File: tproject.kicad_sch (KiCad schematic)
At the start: 0 parts

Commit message: Restore original schematic and project files
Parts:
- added C1, C2, C3, C4: 100n, symbol Device:C
- added C5: 10u, symbol Device:C
- added C6: 10n, symbol Device:C
- added C7, C8: 1u, symbol Device:C
- added FB1: 120R, symbol Device:FerriteBead
- added U1: STM32F103C8T6, Package_QFP:LQFP-48_7x7mm_P0.5mm, symbol MCU_ST_STM32F1:STM32F103C8Tx
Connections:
- new net +3.3V: C1.1, C2.1, C3.1, C4.1, C5.1, C8.1, FB1.2, U1.1 (VBAT), U1.24 (VDD), U1.36 (VDD), U1.48 (VDD)
- new net +3.3VA: C6.1, C7.1, FB1.1, U1.9 (VDDA)
- new net GND: C1.2, C2.2, C3.2, C4.2, C5.2, C6.2, C7.2, C8.2, U1.23 (VSS), U1.35 (VSS), U1.47 (VSS), U1.8 (VSSA)

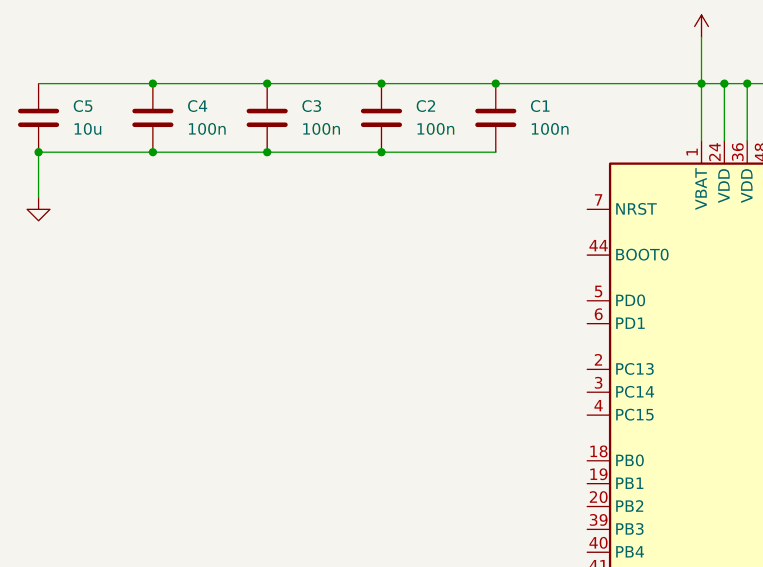
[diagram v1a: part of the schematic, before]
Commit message: Add NRST filter and BOOT0 switch circuit (C9, R1, SW1)
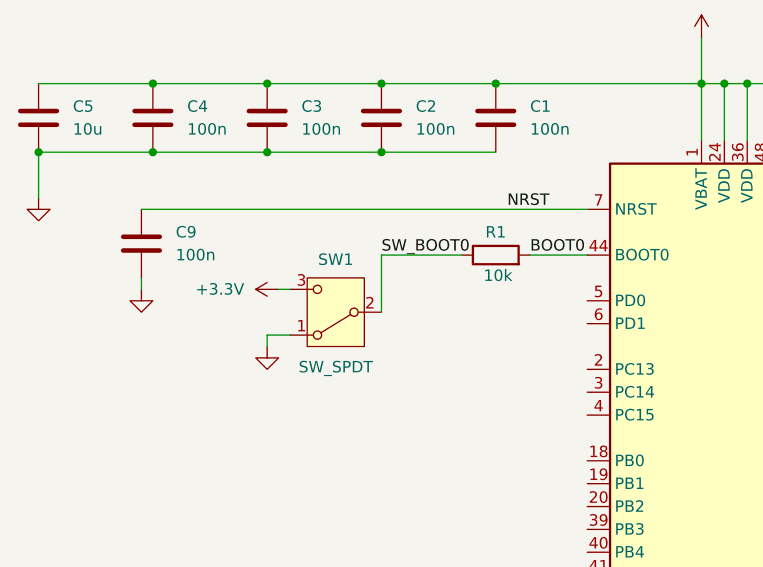
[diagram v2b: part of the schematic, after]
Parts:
- added C9: 100n, symbol Device:C
- added R1: 10k, symbol Device:R
- added SW1: SW_SPDT, symbol Switch:SW_SPDT
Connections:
- net +3.3V: now also SW1.3 (C)
- net GND: now also C9.2, SW1.1 (A)
- net BOOT0: now reaches U1.44 (BOOT0)
- net BOOT0: now also R1.2
- net NRST: now reaches U1.7 (NRST)
- net NRST: now also C9.1
- new net SW_BOOT0: R1.1, SW1.2 (B)

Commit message: Add HSE crystal oscillator circuit (Y1 16MHz, C10/C11 10p) and design note 0003
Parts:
- added C10, C11: 10p, symbol Device:C
- added Y1: 16MHz, symbol Device:Crystal_GND24
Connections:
- net GND: now also C10.2, C11.2, Y1.2 (G), Y1.4 (G)
- net USB_D-: now reaches U1.32 (PA11)
- net USB_D+: now reaches U1.33 (PA12)
- net SDIO: now reaches U1.34 (PA13)
- net SWCLK: now reaches U1.37 (PA14)
- net HSE_IN: now reaches U1.5 (PD0)
- net HSE_IN: now also C11.1, Y1.1
- net HSE_OUT: now reaches U1.6 (PD1)
- net HSE_OUT: now also C10.1, Y1.3

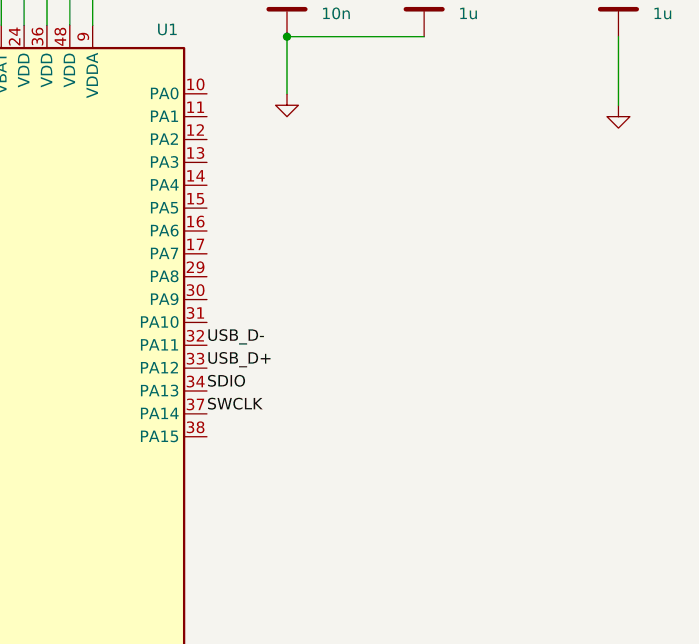
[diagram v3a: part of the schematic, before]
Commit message: Add USB Micro-B interface circuit (J1, R2 1k5 D+ pull-up) and design note 0004
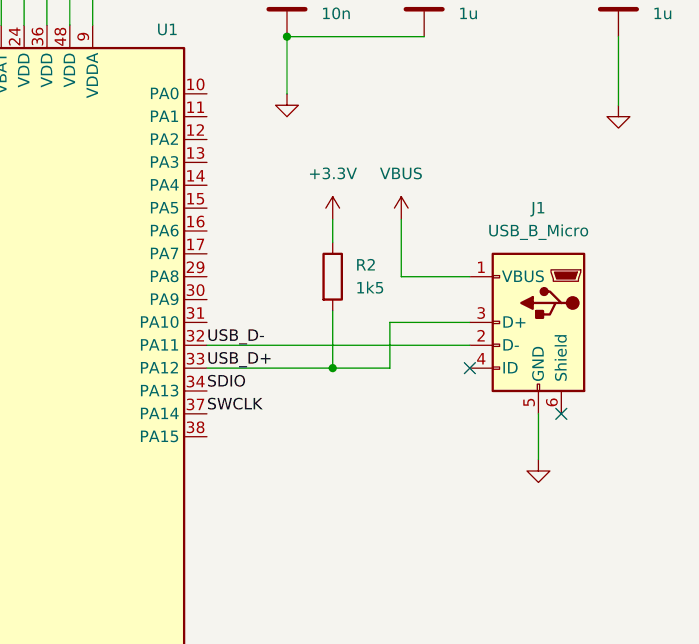
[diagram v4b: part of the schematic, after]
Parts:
- added J1: USB_B_Micro, symbol Connector:USB_B_Micro
- added R2: 1k5, symbol Device:R
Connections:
- net +3.3V: now also R2.1
- net GND: now also J1.5 (GND)
- net USB_D+: now also J1.3 (D+), R2.2
- net USB_D-: now also J1.2 (D-)
- new net VBUS: J1.1 (VBUS)
- no-connect marks 0 -> 2

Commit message: Add 3.3V LDO regulator, power LED, I2C pull-ups, and breakout connectors (U2, C12/C13, D1, R3-R5, J2-J4) and design note 0005
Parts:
- added C12, C13: 22u, symbol Device:C
- added D1: RED, symbol Device:LED
- added J2, J3, J4: Conn_01x04_Pin, symbol Connector:Conn_01x04_Pin
- added R3, R4, R5: 1k5, symbol Device:R
- added U2: AMS1117-3.3, Package_TO_SOT_SMD:SOT-223-3_TabPin2, symbol Regulator_Linear:AMS1117-3.3
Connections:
- net +3.3V: now also C12.1, D1.2 (A), J2.1 (Pin_1), J3.1 (Pin_1), J4.1 (Pin_1), R4.1, R5.1, U2.2 (VO)
- net GND: now also C12.2, C13.2, J2.4 (Pin_4), J3.4 (Pin_4), J4.4 (Pin_4), R3.2, U2.1 (GND)
- net SDIO: now also J2.2 (Pin_2)
- net SWCLK: now also J2.3 (Pin_3)
- net VBUS: now also C13.1, U2.3 (VI)
- net I2C2_SCL: now reaches U1.21 (PB10)
- net I2C2_SCL: now also J4.2 (Pin_2), R4.2
- net I2C2_SDA: now reaches U1.22 (PB11)
- net I2C2_SDA: now also J4.3 (Pin_3), R5.2
- net USART1_TX: now reaches U1.42 (PB6)
- net USART1_TX: now also J3.2 (Pin_2)
- net USART1_RX: now reaches U1.43 (PB7)
- net USART1_RX: now also J3.3 (Pin_3)
- new net PWR_LED_K: D1.1 (K), R3.1
- no-connect marks 2 -> 29
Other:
- moved on the sheet: C1, C10, C11, C2, C3, C4, C5, C6, C7, C8, C9, FB1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

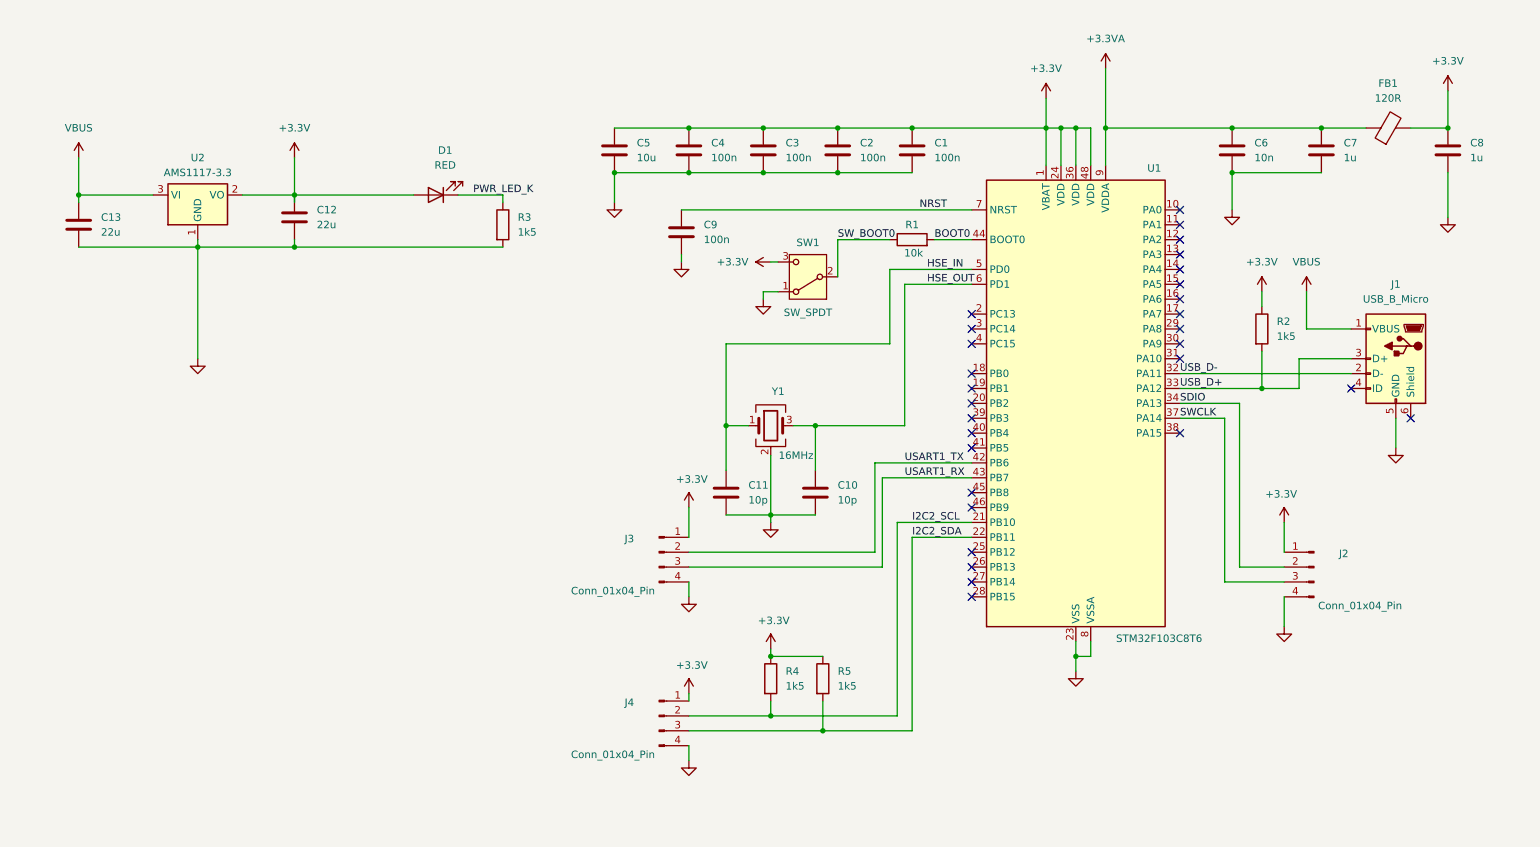
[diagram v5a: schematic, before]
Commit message: Add PWR_FLAG ERC fix, title block, schematic annotations, and component repositioning — design note 0006
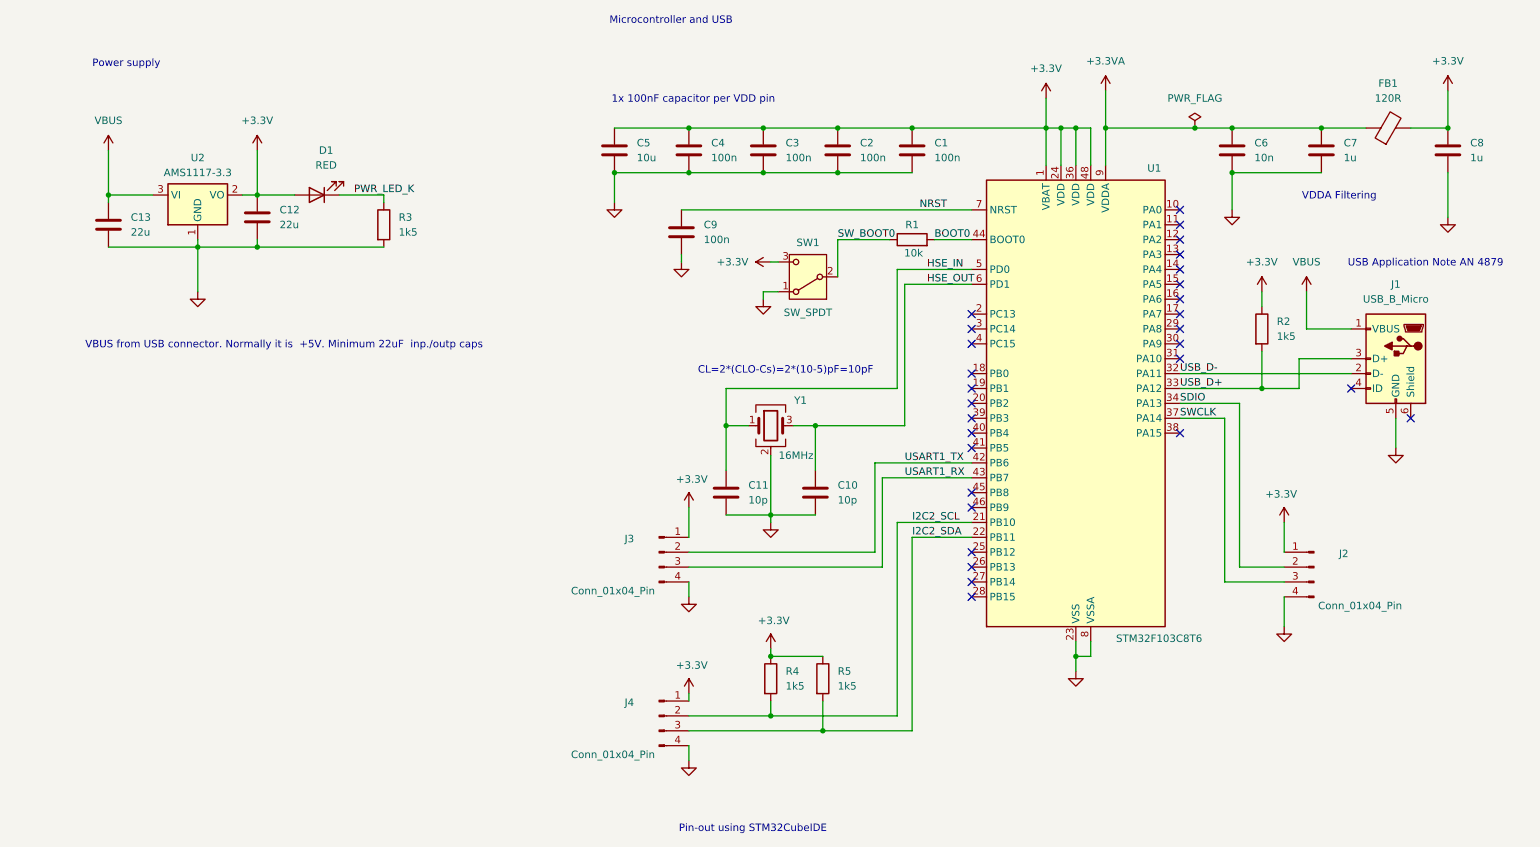
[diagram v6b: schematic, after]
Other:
- note added: "1x 100nF capacitor per VDD pin"
- note added: "CL=2*(CLO-Cs)=2*(10-5)pF=10pF"
- note added: "Microcontroller and USB"
- note added: "Pin-out using STM32CubeIDE"
- note added: "Power supply"
- note added: "USB Application Note AN 4879"
- note added: "VBUS from USB connector. Normally it is +5V. Minimum 22uF inp./outp caps"
- note added: "VDDA Filtering"
- title: (none) -> UDEMY STM32 Demo
- moved on the sheet: C12, C13, D1, R3

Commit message: Re-annotate capacitors and resistors in positional order and update design note 0006
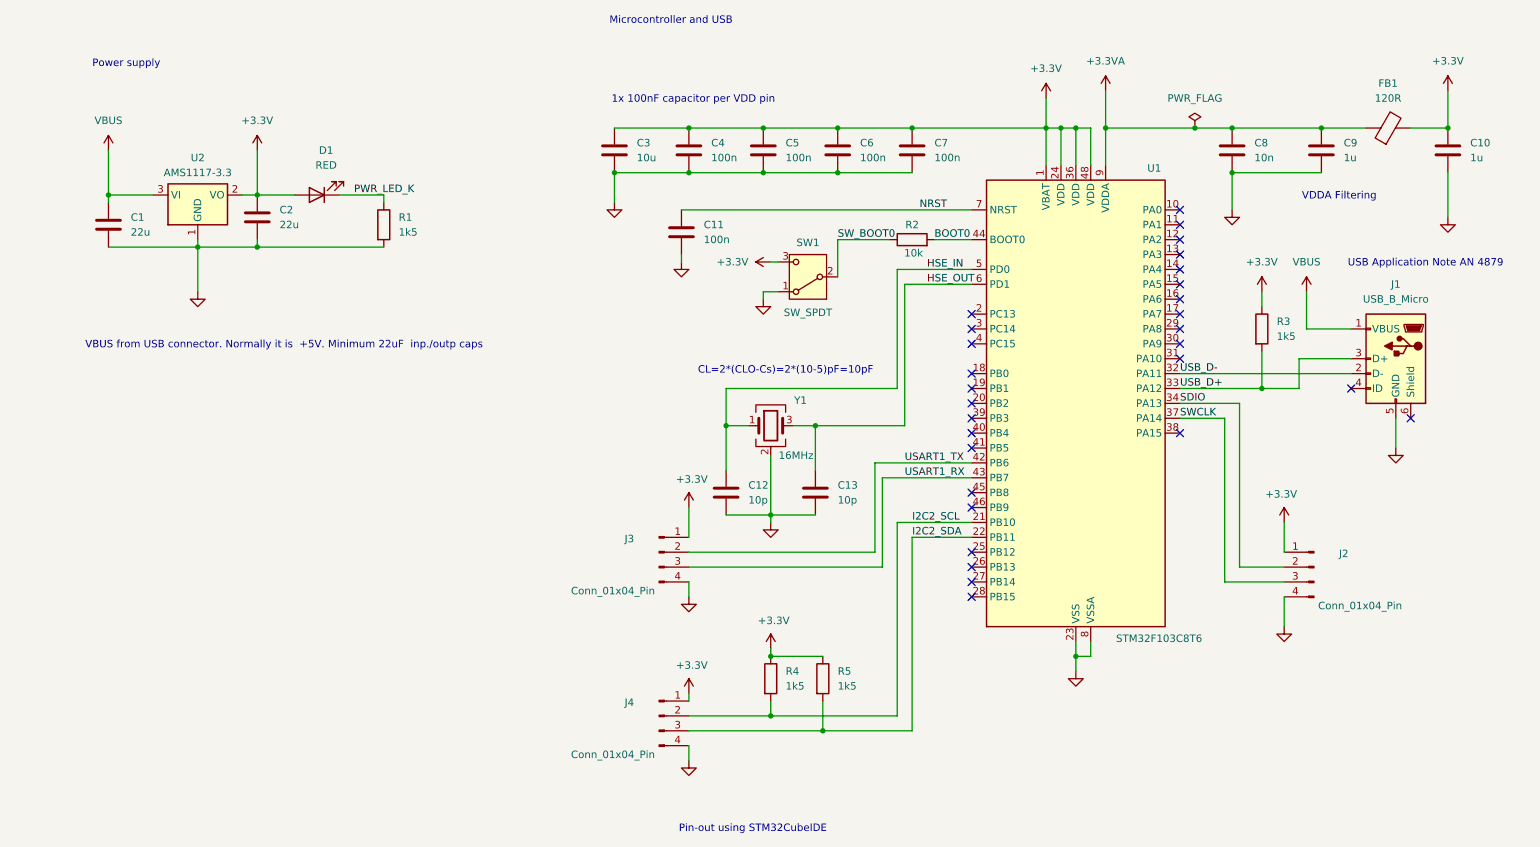
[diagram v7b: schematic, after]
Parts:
- renumbered C13 to C1, C8 to C10, C9 to C11, C11 to C12, C10 to C13, C12 to C2, C5 to C3, C3 to C5, C2 to C6, C1 to C7, C6 to C8, C7 to C9, R3 to R1, R1 to R2, R2 to R3
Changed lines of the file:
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@@
 		(dnp no)
 		(fields_autoplaced yes)
-		(property "Reference" "C13"
+		(property "Reference" "C1"
 			(at 34.29 52.0699 0)
 			(effects
@@
 			(project "tproject"
 				(path "/6a5b46f1-62dd-49ff-8442-d9907adb115c"
-					(reference "C13")
+					(reference "C1")
 					(unit 1)
 				)
@@
 		(dnp no)
 		(fields_autoplaced yes)
-		(property "Reference" "C1"
+		(property "Reference" "C7"
 			(at 171.45 39.3699 0)
 			(effects
@@
 			(project "tproject"
 				(path "/6a5b46f1-62dd-49ff-8442-d9907adb115c"
-					(reference "C1")
+					(reference "C7")
 					(unit 1)
 				)
@@
 		(dnp no)
 		(fields_autoplaced yes)
-		(property "Reference" "C9"
+		(property "Reference" "C11"
 			(at 132.08 53.3399 0)
 			(effects
@@
 			(project "tproject"
 				(path "/6a5b46f1-62dd-49ff-8442-d9907adb115c"
-					(reference "C9")
+					(reference "C11")
 					(unit 1)
 				)
@@
 		(dnp no)
 		(fields_autoplaced yes)
-		(property "Reference" "R2"
+		(property "Reference" "R3"
 			(at 229.87 69.8499 0)
 			(effects
@@
 			(project "tproject"
 				(path "/6a5b46f1-62dd-49ff-8442-d9907adb115c"
-					(reference "R2")
+					(reference "R3")
 					(unit 1)
 				)
@@
 		(dnp no)
 		(fields_autoplaced yes)
-		(property "Reference" "C10"
+		(property "Reference" "C13"
 			(at 154.94 97.7899 0)
 			(effects
@@
 			(project "tproject"
 				(path "/6a5b46f1-62dd-49ff-8442-d9907adb115c"
-					(reference "C10")
+					(reference "C13")
 					(unit 1)
 				)
@@
 		(dnp no)
 		(fields_autoplaced yes)
-		(property "Reference" "C2"
+		(property "Reference" "C6"
 			(at 158.75 39.3699 0)
 			(effects
@@
 			(project "tproject"
 				(path "/6a5b46f1-62dd-49ff-8442-d9907adb115c"
-					(reference "C2")
+					(reference "C6")
 					(unit 1)
 				)
@@
 		(dnp no)
 		(fields_autoplaced yes)
-		(property "Reference" "R3"
+		(property "Reference" "R1"
 			(at 80.01 52.0699 0)
 			(effects
@@
 			(project "tproject"
 				(path "/6a5b46f1-62dd-49ff-8442-d9907adb115c"
-					(reference "R3")
+					(reference "R1")
 					(unit 1)
 				)
@@
 		(dnp no)
 		(fields_autoplaced yes)
-		(property "Reference" "C7"
+		(property "Reference" "C9"
 			(at 241.3 39.3699 0)
 			(effects
@@
 			(project "tproject"
 				(path "/6a5b46f1-62dd-49ff-8442-d9907adb115c"
-					(reference "C7")
+					(reference "C9")
 					(unit 1)
 				)
@@
 		(dnp no)
 		(fields_autoplaced yes)
-		(property "Reference" "C5"
+		(property "Reference" "C3"
 			(at 120.65 39.3699 0)
 			(effects
@@
 			(project "tproject"
 				(path "/6a5b46f1-62dd-49ff-8442-d9907adb115c"
-					(reference "C5")
+					(reference "C3")
 					(unit 1)
 				)
@@
 		(dnp no)
 		(fields_autoplaced yes)
-		(property "Reference" "C12"
+		(property "Reference" "C2"
 			(at 59.69 50.7999 0)
 			(effects
@@
 			(project "tproject"
 				(path "/6a5b46f1-62dd-49ff-8442-d9907adb115c"
-					(reference "C12")
+					(reference "C2")
 					(unit 1)
 				)
@@
 		(dnp no)
 		(fields_autoplaced yes)
-		(property "Reference" "C3"
+		(property "Reference" "C5"
 			(at 146.05 39.3699 0)
 			(effects
@@
 			(project "tproject"
 				(path "/6a5b46f1-62dd-49ff-8442-d9907adb115c"
-					(reference "C3")
+					(reference "C5")
 					(unit 1)
 				)
@@
 		(dnp no)
 		(fields_autoplaced yes)
-		(property "Reference" "C11"
+		(property "Reference" "C12"
 			(at 139.7 97.7899 0)
 			(effects
@@
 			(project "tproject"
 				(path "/6a5b46f1-62dd-49ff-8442-d9907adb115c"
-					(reference "C11")
+					(reference "C12")
 					(unit 1)
 				)
@@
 		(dnp no)
 		(fields_autoplaced yes)
-		(property "Reference" "C8"
+		(property "Reference" "C10"
 			(at 262.89 39.3699 0)
 			(effects
@@
 			(project "tproject"
 				(path "/6a5b46f1-62dd-49ff-8442-d9907adb115c"
-					(reference "C8")
+					(reference "C10")
 					(unit 1)
 				)
@@
 		(on_board yes)
 		(dnp no)
-		(property "Reference" "R1"
+		(property "Reference" "R2"
 			(at 167.64 53.34 90)
 			(effects
@@
 			(project "tproject"
 				(path "/6a5b46f1-62dd-49ff-8442-d9907adb115c"
-					(reference "R1")
+					(reference "R2")
 					(unit 1)
 				)
@@
 		(dnp no)
 		(fields_autoplaced yes)
-		(property "Reference" "C6"
+		(property "Reference" "C8"
 			(at 226.06 39.3699 0)
 			(effects
@@
 			(project "tproject"
 				(path "/6a5b46f1-62dd-49ff-8442-d9907adb115c"
-					(reference "C6")
+					(reference "C8")
 					(unit 1)
 				)
